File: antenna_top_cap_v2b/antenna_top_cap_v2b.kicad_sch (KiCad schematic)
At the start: 43 parts, among them J1 DEBUG, J10 WDT Disable Jumper, J11 DF11-4DP-2DSA, J12 USB_C_Receptacle_USB2.0_16P, J13 DNP, J2 Battery Charge Bypass, J3 FC Reset Jumper, J4 FC USB Bootselect Jumper, J5 Conn_Coaxial, J8 USB_C_Receptacle_USB2.0_16P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

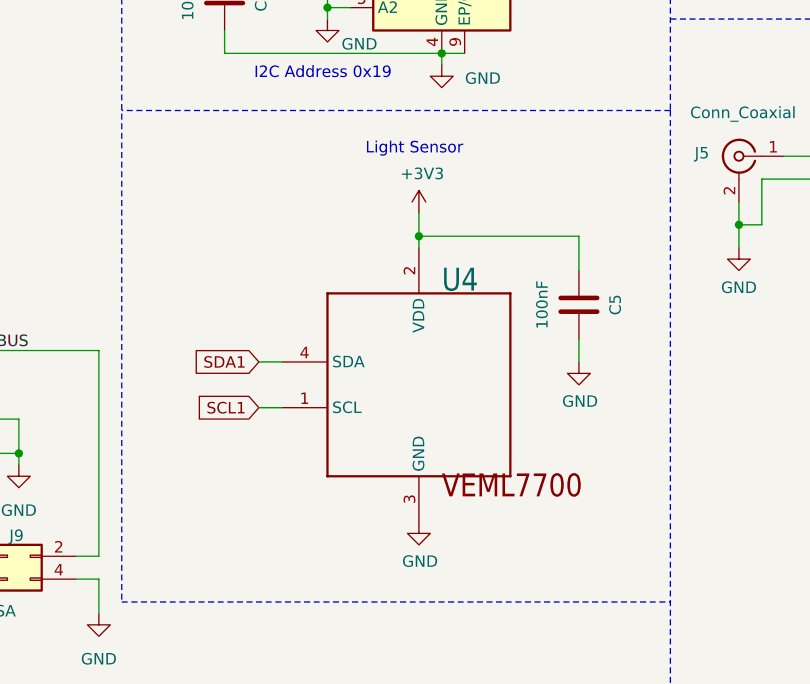
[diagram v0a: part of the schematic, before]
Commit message: V2b: Switched From VEML7700 to VEML61
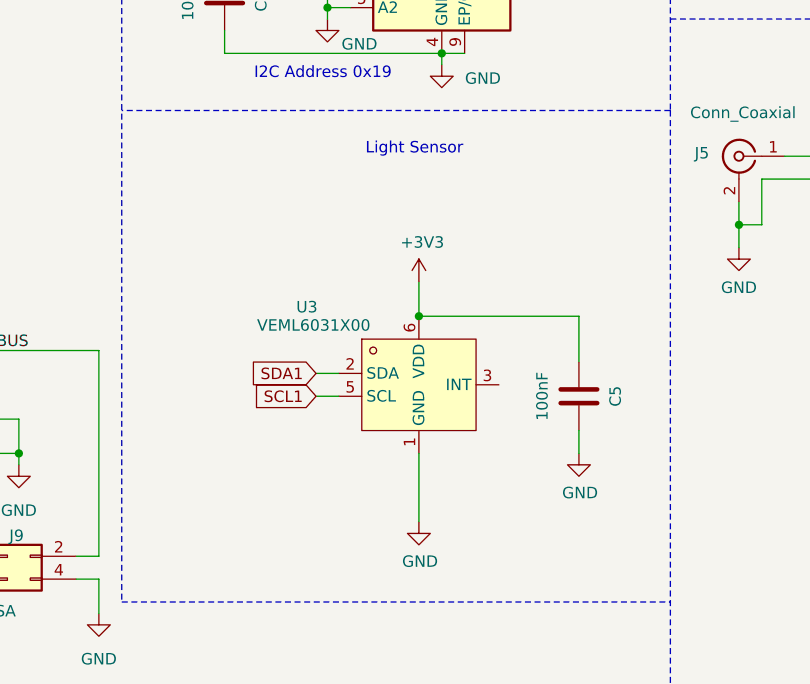
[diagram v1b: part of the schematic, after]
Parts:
- removed U4: VEML7700, VEML7700-TT:XDCR_VEML7700-TT, symbol Adafruit VEML7700-eagle-import:VEML7700
- added U3: VEML6031X00, easyeda2kicad:SENSOR-SMD_VEML6031X00, symbol easyeda2kicad:VEML6031X00
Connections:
- net +3V3: now also U3.6 (VDD)
- net GND: now also U3.1 (GND), U3.4 (GND)
- net SCL0: now also U3.5 (SCL)
- net SDA0: now also U3.2 (SDA)
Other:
- moved on the sheet: C5
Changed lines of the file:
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@@
 	)
 	(junction
+		(at 110.49 125.73)
+		(diameter 0)
+		(color 0 0 0 0)
+	)
+	(junction
 		(at 270.51 149.86)
 		(diameter 0)
@@
 	)
 	(junction
-		(at 110.49 116.84)
-		(diameter 0)
-		(color 0 0 0 0)
-	)
-	(junction
 		(at 245.11 27.94)
 		(diameter 0)
@@
 	(wire
 		(pts
-			(xy 128.27 116.84) (xy 128.27 120.65)
+			(xy 128.27 125.73) (xy 128.27 130.81)
 		)
 		(stroke
@@
 	(wire
 		(pts
-			(xy 110.49 116.84) (xy 128.27 116.84)
+			(xy 110.49 125.73) (xy 128.27 125.73)
 		)
 		(stroke
@@
 	(wire
 		(pts
-			(xy 128.27 128.27) (xy 128.27 130.81)
+			(xy 128.27 138.43) (xy 128.27 140.97)
 		)
 		(stroke
@@
 	(wire
 		(pts
-			(xy 92.71 135.89) (xy 95.25 135.89)
-		)
-		(stroke
-			(width 0)
-			(type default)
-		)
-	)
-	(wire
-		(pts
 			(xy 22.86 179.07) (xy 22.86 175.26)
 		)
@@
 	(wire
 		(pts
+			(xy 110.49 140.97) (xy 110.49 148.59)
+		)
+		(stroke
+			(width 0)
+			(type default)
+		)
+	)
+	(wire
+		(pts
 			(xy 269.24 27.94) (xy 269.24 25.4)
 		)
@@
 		)
 	)
+	(wire
+		(pts
+			(xy 99.06 134.62) (xy 101.6 134.62)
+		)
+		(stroke
+			(width 0)
+			(type default)
+		)
+	)
 	(polyline
 		(pts
@@
 	(wire
 		(pts
-			(xy 110.49 116.84) (xy 110.49 118.11)
+			(xy 110.49 121.92) (xy 110.49 125.73)
 		)
 		(stroke
@@
 	(wire
 		(pts
-			(xy 110.49 114.3) (xy 110.49 116.84)
-		)
-		(stroke
-			(width 0)
-			(type default)
-		)
-	)
-	(wire
-		(pts
 			(xy 143.637 82.55) (xy 162.56 82.55)
 		)
@@
 	(wire
 		(pts
-			(xy 95.25 130.81) (xy 92.71 130.81)
+			(xy 101.6 132.08) (xy 99.06 132.08)
 		)
 		(stroke
@@
 	(global_label "SDA1"
 		(shape input)
-		(at 92.71 130.81 180)
+		(at 99.06 132.08 180)
 		(fields_autoplaced yes)
 		(effects
@@
 		)
 		(property "Intersheetrefs" "${INTERSHEET_REFS}"
-			(at 84.9472 130.81 0)
+			(at 91.2972 132.08 0)
 			(effects
 				(font
@@
 	(global_label "SCL1"
 		(shape input)
-		(at 92.71 135.89 180)
+		(at 99.06 134.62 180)
 		(fields_autoplaced yes)
 		(effects
@@
 		)
 		(property "Intersheetrefs" "${INTERSHEET_REFS}"
-			(at 85.0077 135.89 0)
+			(at 91.3577 134.62 0)
 			(effects
 				(font
@@
 	(symbol
 		(lib_id "solar-panel-side-Z-rescue:+3.3V-power")
-		(at 110.49 114.3 0)
+		(at 110.49 121.92 0)
 		(unit 1)
 		(exclude_from_sim no)
@@
 		(dnp no)
 		(property "Reference" "#PWR0101"
-			(at 110.49 118.11 0)
+			(at 110.49 125.73 0)
 			(effects
 				(font
@@
 		)
 		(property "Value" "+3V3"
-			(at 110.871 109.9058 0)
+			(at 110.871 117.5258 0)
 			(effects
 				(font
@@
 		)
 		(property "Footprint" ""
-			(at 110.49 114.3 0)
+			(at 110.49 121.92 0)
 			(effects
 				(font
@@
 		)
 		(property "Datasheet" ""
-			(at 110.49 114.3 0)
+			(at 110.49 121.92 0)
 			(effects
 				(font
@@
 		)
 		(property "Description" ""
-			(at 110.49 114.3 0)
+			(at 110.49 121.92 0)
 			(effects
 				(font
@@
 	)
 	(symbol
+		(lib_id "easyeda2kicad:VEML6031X00")
+		(at 110.49 133.35 0)
+		(unit 1)
+		(exclude_from_sim no)
+		(in_bom yes)
+		(on_board yes)
+		(dnp no)
+		(property "Reference" "U3"
+			(at 98.044 124.714 0)
+			(effects
+				(font
+					(size 1.27 1.27)
+				)
+			)
+		)
+		(property "Value" "VEML6031X00"
+			(at 98.806 126.746 0)
+			(effects
+				(font
+					(size 1.27 1.27)
+				)
+			)
+		)
+		(property "Footprint" "easyeda2kicad:SENSOR-SMD_VEML6031X00"
+			(at 110.49 143.51 0)
+			(effects
+				(font
+					(size 1.27 1.27)
+				)
+				(hide yes)
+			)
+		)
+		(property "Datasheet" ""
+			(at 110.49 133.35 0)
+			(effects
+				(font
+					(size 1.27 1.27)
+				)
+				(hide yes)
+			)
+		)
+		(property "Description" ""
+			(at 110.49 133.35 0)
+			(effects
+				(font
+					(size 1.27 1.27)
+				)
+				(hide yes)
+			)
+		)
+		(property "LCSC Part" "C3678616"
+			(at 110.49 146.05 0)
+			(effects
+				(font
+					(size 1.27 1.27)
+				)
+				(hide yes)
+			)
+		)
+		(pin "2"
+		)
+		(pin "3"
+		)
+		(pin "4"
+		)
+		(pin "1"
+		)
+		(pin "5"
+		)
+		(pin "6"
+		)
+		(instances
+			(project ""
+				(path "/e63e39d7-6ac0-4ffd-8aa3-1841a4541b55"
+					(reference "U3")
+					(unit 1)
+				)
+			)
+		)
+	)
+	(symbol
 		(lib_id "Adafruit VL6180 Time of Flight Sensor-eagle-import:GND")
 		(at 223.52 90.17 0)
@@
 	(symbol
 		(lib_id "power:GND")
-		(at 128.27 130.81 0)
+		(at 128.27 140.97 0)
 		(unit 1)
 		(exclude_from_sim no)
@@
 		(dnp no)
 		(property "Reference" "#PWR08"
-			(at 128.27 137.16 0)
+			(at 128.27 147.32 0)
 			(effects
 				(font
@@
 		)
 		(property "Value" "GND"
-			(at 128.397 135.2042 0)
+			(at 128.397 145.3642 0)
 			(effects
 				(font
@@
 		)
 		(property "Footprint" ""
-			(at 128.27 130.81 0)
+			(at 128.27 140.97 0)
 			(effects
 				(font
@@
 		)
 		(property "Datasheet" ""
-			(at 128.27 130.81 0)
+			(at 128.27 140.97 0)
 			(effects
 				(font
@@
 		)
 		(property "Description" ""
-			(at 128.27 130.81 0)
+			(at 128.27 140.97 0)
 			(effects
 				(font
@@
 	(symbol
 		(lib_id "Device:C")
-		(at 128.27 124.46 0)
+		(at 128.27 134.62 0)
 		(unit 1)
 		(exclude_from_sim no)
@@
 		(dnp no)
 		(property "Reference" "C5"
-			(at 132.334 124.46 90)
+			(at 132.334 134.62 90)
 			(effects
 				(font
@@
 		)
 		(property "Value" "100nF"
-			(at 124.206 124.46 90)
+			(at 124.206 134.62 90)
 			(effects
 				(font
@@
 		)
 		(property "Footprint" "Capacitor_SMD:C_0805_2012Metric"
-			(at 129.2352 128.27 0)
+			(at 129.2352 138.43 0)
 			(effects
 				(font
@@
 		)
 		(property "Datasheet" "~"
-			(at 128.27 124.46 0)
+			(at 128.27 134.62 0)
 			(effects
 				(font
@@
 		)
 		(property "Description" ""
-			(at 128.27 124.46 0)
+			(at 128.27 134.62 0)
 			(effects
 				(font
@@
 					(unit 1)
 				)
-			)
-		)
-	)
-	(symbol
-		(lib_id "Adafruit VEML7700-eagle-import:VEML7700")
-		(at 110.49 133.35 0)
-		(unit 1)
-		(exclude_from_sim no)
-		(in_bom yes)
-		(on_board yes)
-		(dnp no)
-		(property "Reference" "U4"
-			(at 113.03 123.19 0)
-			(effects
-				(font
-					(size 2.54 2.159)
-				)
-				(justify left bottom)
-			)
-		)
-		(property "Value" "VEML7700"
-			(at 110.49 133.35 0)
-			(effects
-				(font
-					(size 1.27 1.27)
-				)
-				(hide yes)
-			)
-		)
-		(property "Footprint" "VEML7700-TT:XDCR_VEML7700-TT"
-			(at 110.49 133.35 0)
-			(effects
-				(font
-					(size 1.27 1.27)
-				)
-				(hide yes)
-			)
-		)
-		(property "Datasheet" ""
-			(at 110.49 133.35 0)
-			(effects
-				(font
-					(size 1.27 1.27)
-				)
-				(hide yes)
-			)
-		)
-		(property "Description" ""
-			(at 110.49 133.35 0)
-			(effects
-				(font
-					(size 1.27 1.27)
-				)
-				(hide yes)
-			)
-		)
-		(pin "1"
-		)
-		(pin "2"
-		)
-		(pin "3"
-		)
-		(pin "4"
-		)
-		(instances
-			(project "antenna_top_cap_v2a"
-				(path "/e63e39d7-6ac0-4ffd-8aa3-1841a4541b55"
-					(reference "U4")
-					(unit 1)
-				)

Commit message: As ORdered For V3 Pro
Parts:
- removed J5: Conn_Coaxial, Connector_Coaxial:SMA_Amphenol_901-144_Vertical, symbol Connector:Conn_Coaxial
- removed U16: MCP9808T-E/MS, Package_SO:MSOP-8-1EP_3x3mm_P0.65mm_EP1.5x1.8mm_ThermalVias, symbol Sensor_Temperature:MCP9808_DFN
- removed U5: HHM1591D1, easyeda2kicad:XFMR-SMD_HHM1591D1, symbol easyeda2kicad:HHM1591D1
- added B1: ATB2012-50011-T000, easyeda2kicad:XFMR-SMD_ATB2012-50011-T000, symbol easyeda2kicad:ATB2012-50011-T000
- added R10, R11, R8, R9: 10k, Resistor_SMD:R_0603_1608Metric, symbol mainboard:RESISTOR0603
- added RF1: KH-MMCX-Z, easyeda2kicad:MMCX-TH_KH-MMCX-Z, symbol easyeda2kicad:KH-MMCX-Z
- added U4: TMP112xxDRL, Package_TO_SOT_SMD:SOT-563, symbol Sensor_Temperature:TMP112xxDRL
- added U6: TCA4311ADGKR, easyeda2kicad:MSOP-8_L3.0-W3.0-P0.65-LS5.0-BL, symbol easyeda2kicad:TCA4311ADGKR
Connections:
- net +3V3: now also R10.1, R11.1, R8.1, R9.1, U4.5 (V+), U6.8 (VCC)
- net GND: now also B1.2, RF1.1, RF1.2, RF1.3, RF1.4, U4.2 (GND), U4.3 (ALERT), U4.4 (ADD0), U6.4 (GND)
- net SCL0: now also U6.3 (SCLIN); no longer Q1.6 (D), R3.8 (2), U3.5 (SCL)
- net SDA0: now also U6.6 (SDAIN); no longer Q1.3 (D), R3.7 (2), U3.2 (SDA)
- net at J6.1 (tape_1): now also B1.3
- net at J6.2 (tape_2): now also B1.4 (B.P.50)
- new net: R8.2, U6.1 (EN)
- new net: R11.2, U6.5 (READY)
- new net: B1.1 (U.P.50), RF1.5
- new net SCL1: Q1.6 (D), R10.2, R3.8 (2), U3.5 (SCL), U4.1 (SCL), U6.2 (SCLOUT)
- new net SDA1: Q1.3 (D), R3.7 (2), R9.2, U3.2 (SDA), U4.6 (SDA), U6.7 (SDAOUT)
- no-connect marks 15 -> 13
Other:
- moved on the sheet: C43, J6
